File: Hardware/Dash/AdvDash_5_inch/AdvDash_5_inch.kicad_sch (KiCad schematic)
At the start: 1 part, among them J1 MICROMOD-2222

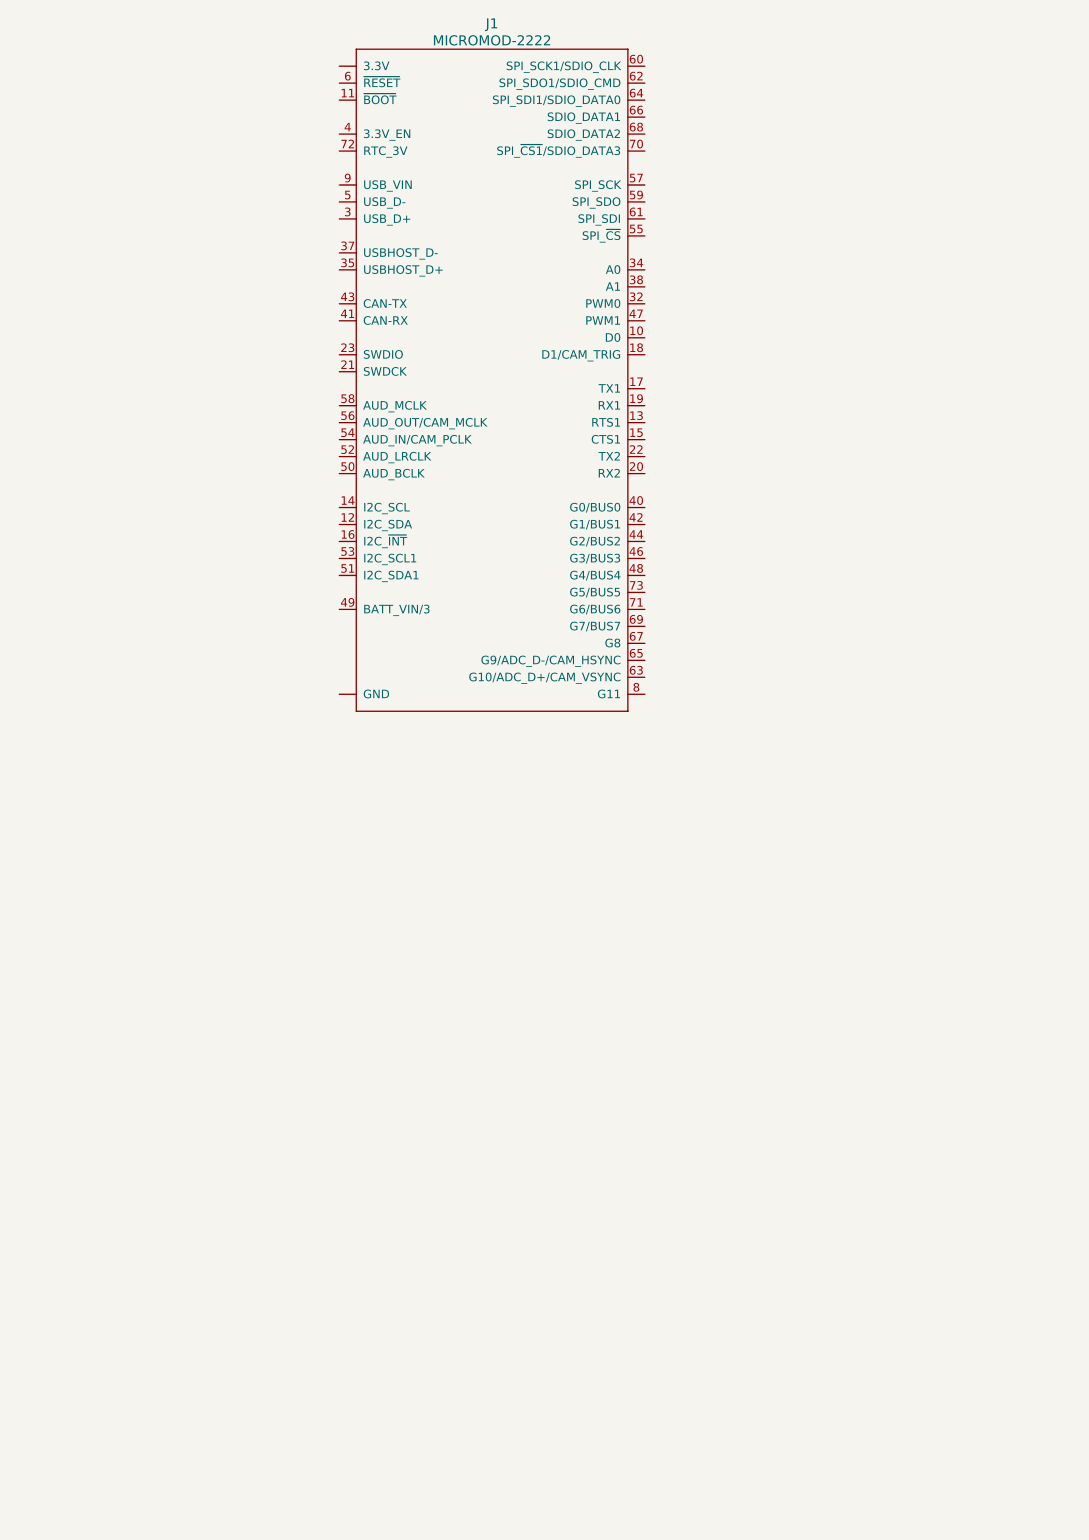
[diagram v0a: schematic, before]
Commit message: R0.1.0 PCB added
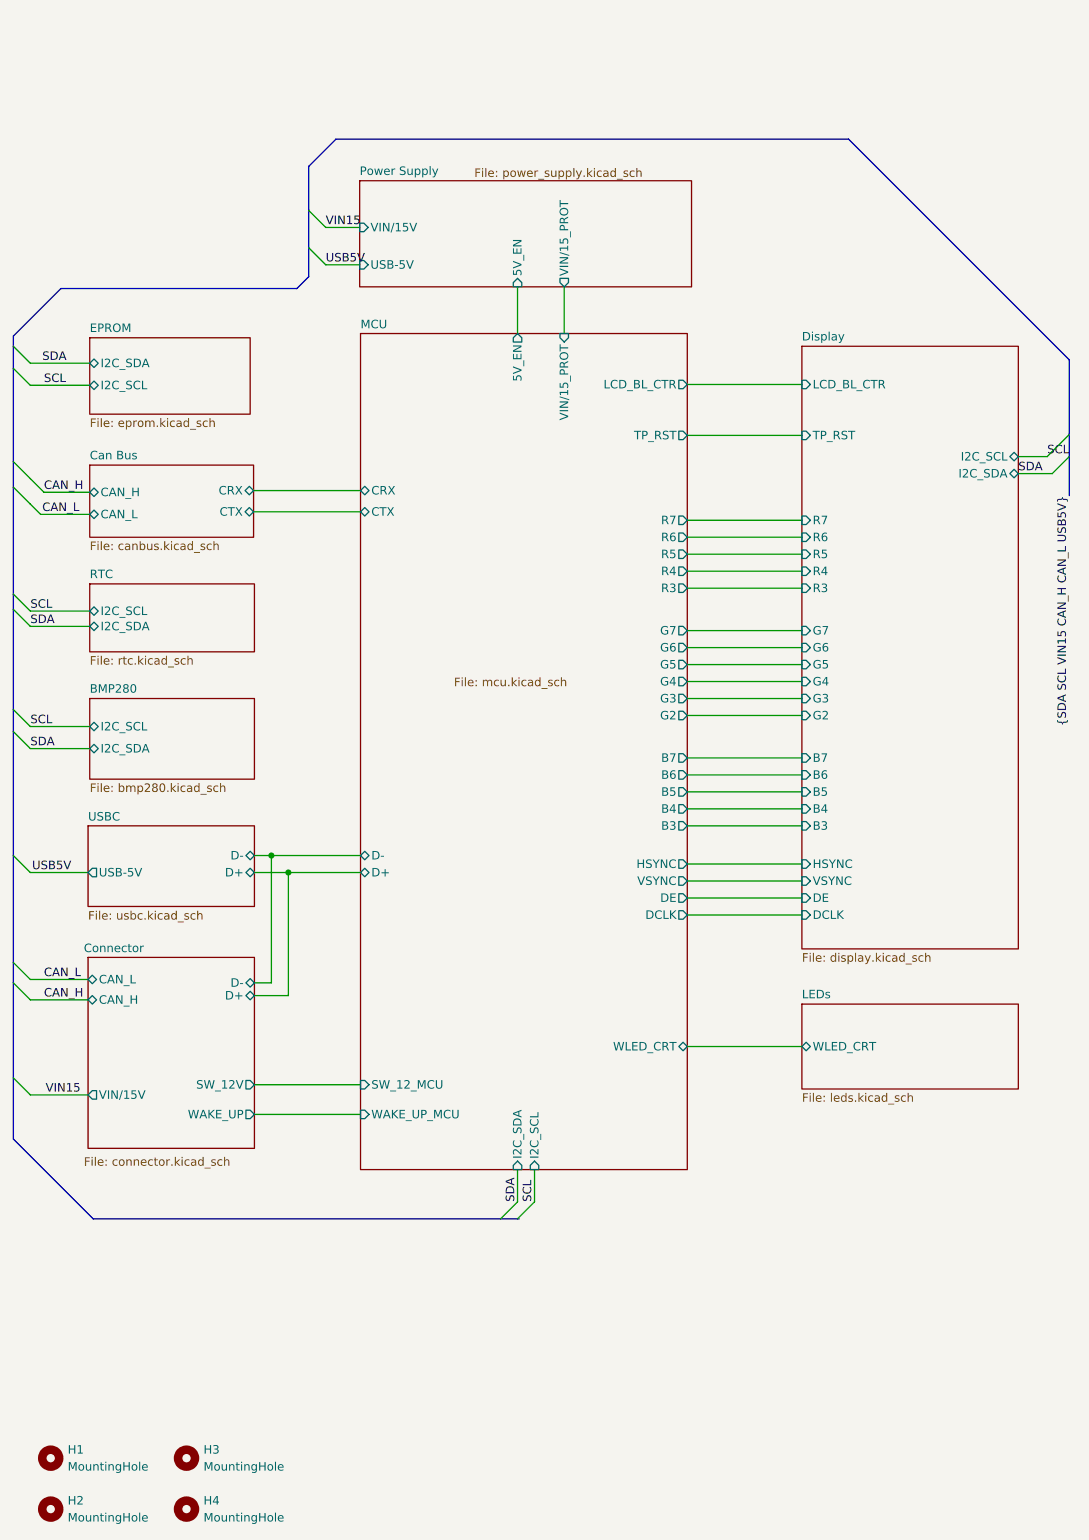
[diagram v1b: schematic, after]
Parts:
- removed J1: MICROMOD-2222, M.2-CARD-E-22:M.2-CARD-E-22, symbol MicroMod_Processor_Board (2):MICROMOD-2222
- added H1, H2, H3, H4: MountingHole, MountingHole:MountingHole_3.2mm_M3_Pad_Via, symbol Mechanical:MountingHole
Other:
- added sheet BMP280 (bmp280.kicad_sch)
- added sheet Can Bus (canbus.kicad_sch)
- added sheet Connector (connector.kicad_sch)
- added sheet Display (display.kicad_sch)
- added sheet EPROM (eprom.kicad_sch)
- added sheet LEDs (leds.kicad_sch)
- added sheet MCU (mcu.kicad_sch)
- added sheet Power Supply (power_supply.kicad_sch)
- added sheet RTC (rtc.kicad_sch)
- added sheet USBC (usbc.kicad_sch)

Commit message: PCB R0.1.0
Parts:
- H1, H2, H3, H4: footprint MountingHole:MountingHole_3.2mm_M3_Pad_Via -> MountingHole:MountingHole_3.2mm_M3_DIN965_Pad_TopBottom
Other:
- company: (none) -> ADV.ECU - GNVPerformance
- title: (none) -> Root Sheet

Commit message: :bug: PCB R0.2.0 Ready, change log in kicad files
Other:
- sheet Display ports: added TP_RST_2; removed none
- sheet LEDs ports: added WLED_CLK; removed none
- sheet MCU ports: added TP_RST_2, WLED_CLK; removed none
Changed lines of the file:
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@@
+    (stroke (width 0) (type default))
+  )
+  (wire (pts (xy 132.08 180.34) (xy 149.225 180.34))
     (stroke (width 0) (type default))
   )
@@
   )
   (bus (pts (xy 156.21 41.402) (xy 189.23 74.422))
+    (stroke (width 0) (type default))
+  )
+  (wire (pts (xy 132.08 88.265) (xy 149.225 88.265))
     (stroke (width 0) (type default))
   )
@@
       (effects (font (size 1.27 1.27)) (justify right))
     )
+    (pin "TP_RST_2" input (at 132.08 88.265 0)
+      (effects (font (size 1.27 1.27)) (justify right))
+    )
+    (pin "WLED_CLK" bidirectional (at 132.08 180.34 0)
+      (effects (font (size 1.27 1.27)) (justify right))
+    )
     (instances
       (project "AdvDash_5_inch"
@@
       (effects (font (size 1.27 1.27)) (justify left))
     )
+    (pin "WLED_CLK" bidirectional (at 149.225 180.34 180)
+      (effects (font (size 1.27 1.27)) (justify left))
+    )
     (instances
       (project "AdvDash_5_inch"
@@
       (effects (font (size 1.27 1.27)) (justify left))
     )
+    (pin "TP_RST_2" output (at 149.225 88.265 180)
+      (effects (font (size 1.27 1.27)) (justify left))
+    )
